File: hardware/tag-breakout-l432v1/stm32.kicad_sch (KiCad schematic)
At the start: 14 parts, among them J3 Conn_01x17, J4 Conn_01x17, J5 Conn_01x02_Male, Q1 Q_NPN_BEC, U3 stm32l432, U6 RV-3028-C7

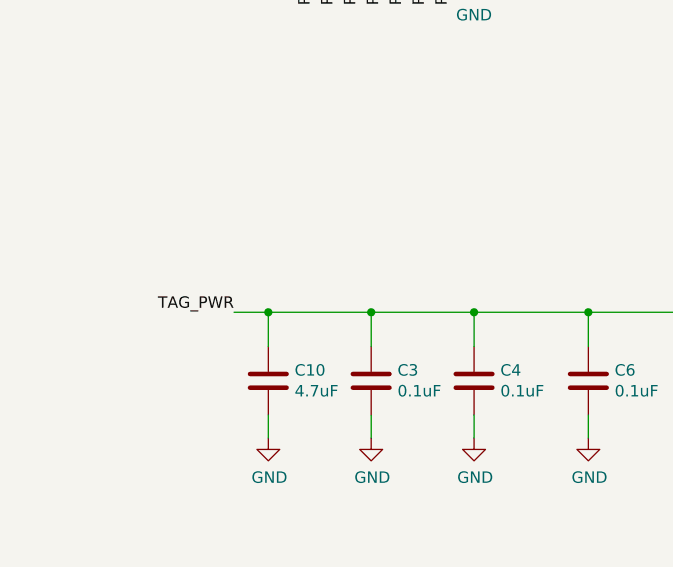
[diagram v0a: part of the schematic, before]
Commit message: checkpoint -- order compass proto board
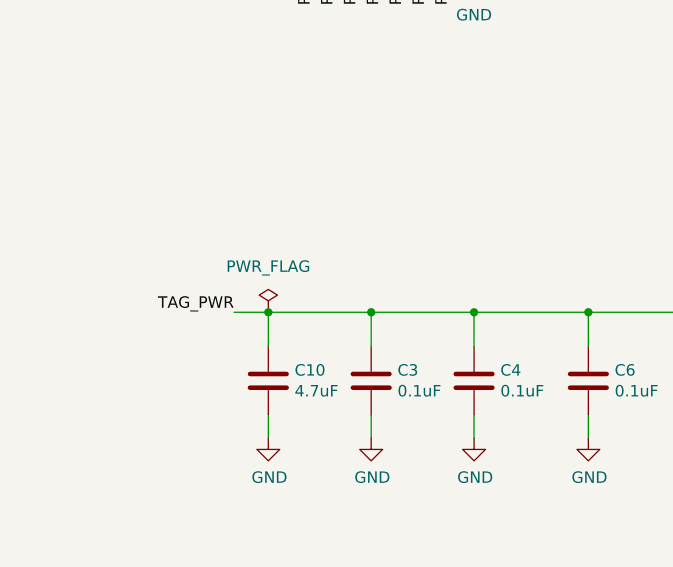
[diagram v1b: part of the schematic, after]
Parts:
- U3: LCSC (none) -> C94784
- U6: LCSC (none) -> C3019759
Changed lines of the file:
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@@
 			)
 		)
-		(property "Description" ""
+		(property "Description" "Power symbol creates a global label with name \"GND\" , ground"
 			(at 58.42 166.37 0)
 			(effects
@@
 			)
 		)
-		(property "Description" ""
+		(property "Description" "Power symbol creates a global label with name \"GND\" , ground"
 			(at 69.85 166.37 0)
 			(effects
@@
 			)
 		)
-		(property "Description" ""
+		(property "Description" "Power symbol creates a global label with name \"GND\" , ground"
 			(at 81.28 166.37 0)
 			(effects
@@
 			)
 		)
-		(property "Description" ""
+		(property "Description" "Power symbol creates a global label with name \"GND\" , ground"
 			(at 93.98 166.37 0)
 			(effects
@@
 			)
 		)
-		(property "Description" ""
+		(property "Description" "Power symbol creates a global label with name \"GND\" , ground"
 			(at 106.68 166.37 0)
 			(effects
@@
 			)
 		)
-		(property "Description" ""
+		(property "Description" "Power symbol creates a global label with name \"GND\" , ground"
 			(at 140.335 169.545 0)
 			(effects
@@
 			)
 		)
-		(property "Description" ""
+		(property "Description" "Power symbol creates a global label with name \"GND\" , ground"
 			(at 156.845 169.545 0)
 			(effects
@@
 			)
 		)
+		(property "LCSC" "C3019759 "
+			(at 255.905 149.86 0)
+			(effects
+				(font
+					(size 1.27 1.27)
+				)
+				(hide yes)
+			)
+		)
 		(pin "1"
 		)
@@
 			)
 		)
-		(property "Description" ""
+		(property "Description" "Power symbol creates a global label with name \"GND\" , ground"
 			(at 224.79 156.21 0)
 			(effects
@@
 			)
 		)
-		(property "Description" ""
+		(property "Description" "Power symbol creates a global label with name \"GND\" , ground"
 			(at 213.36 157.48 0)
 			(effects
@@
 			)
 		)
-		(property "Description" ""
+		(property "Description" "Power symbol creates a global label with name \"GND\" , ground"
 			(at 271.145 156.21 0)
 			(effects
@@
 			)
 		)
-		(property "Description" ""
+		(property "Description" "Power symbol creates a global label with name \"GND\" , ground"
 			(at 211.455 97.79 0)
 			(effects
@@
 			)
 		)
-		(property "Description" ""
+		(property "Description" "Power symbol creates a global label with name \"GND\" , ground"
 			(at 189.865 97.79 0)
 			(effects
@@
 			)
 		)
+		(property "LCSC" "C94784"
+			(at 40.64 71.755 0)
+			(effects
+				(font
+					(size 1.27 1.27)
+				)
+				(hide yes)
+			)
+		)
 		(pin "31"
 		)
@@
 	)
 	(symbol
-		(lib_name "GND_1")
 		(lib_id "power:GND")
 		(at 81.28 114.935 0)
@@
 	)
 	(symbol
-		(lib_name "GND_1")
 		(lib_id "power:GND")
 		(at 55.88 45.085 0)
@@
 					(unit 1)
 				)
+			)
+		)
+	)
+	(symbol
+		(lib_id "power:PWR_FLAG")
+		(at 58.42 152.4 0)
+		(unit 1)
+		(exclude_from_sim no)
+		(in_bom yes)
+		(on_board yes)
+		(dnp no)
+		(fields_autoplaced yes)
+		(property "Reference" "#FLG2"
+			(at 58.42 150.495 0)
+			(effects
+				(font
+					(size 1.27 1.27)
+				)
+				(hide yes)
+			)
+		)
+		(property "Value" "PWR_FLAG"
+			(at 58.42 147.32 0)
+			(effects
+				(font
+					(size 1.27 1.27)
+				)
+			)
+		)
+		(property "Footprint" ""
+			(at 58.42 152.4 0)
+			(effects
+				(font
+					(size 1.27 1.27)
+				)
+				(hide yes)
+			)
+		)
+		(property "Datasheet" "~"
+			(at 58.42 152.4 0)
+			(effects
+				(font
+					(size 1.27 1.27)
+				)
+				(hide yes)
+			)
+		)
+		(property "Description" "Special symbol for telling ERC where power comes from"
+			(at 58.42 152.4 0)
+			(effects
+				(font
+					(size 1.27 1.27)
+				)
+				(hide yes)
+			)
+		)
+		(pin "1"
+		)
+		(instances
+			(project ""
+				(path "/2d561ecb-394a-4bb7-a154-94e4285b4f36/00000000-0000-0000-0000-00005fa00cea"
+					(reference "#FLG2")
+					(unit 1)
+				)

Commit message: update proto boards
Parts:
- J3, J4: footprint Connector_PinSocket_2.54mm:PinSocket_1x17_P2.54mm_Vertical -> library:PinHeader_1x17_P2.54mm_Vertical_Staggered
- U6: symbol tag-breakout-v2-rescue:RV-3028-C7-gpsparts -> tag-library:RV-3028-C7
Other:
- moved on the sheet: C5, J3, J4, Q1, U3, U6

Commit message: checkpoint
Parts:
- removed J5: Conn_01x02_Male, Connector_PinHeader_2.54mm:PinHeader_1x02_P2.54mm_Vertical, symbol Connector_Generic:Conn_01x02
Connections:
- net TAG_PWR is gone; now on net TAG_3V3: C10.1, C3.1, C4.1, C6.1, C7.1, C9.1, J3.7 (Pin_7), J4.1 (Pin_1), U3.1 (VDD), U3.17 (VDD), U3.5 (VDDA/VREF+), U6.7 (VDD)
